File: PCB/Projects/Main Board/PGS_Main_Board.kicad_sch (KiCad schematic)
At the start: 119 parts, among them J1 SM02B-SURS-TF_LF__SN_, J2 SM02B-SURS-TF_LF__SN_, J3 Molex 505110-0892, J5 Molex 505110-0892, J6 Molex 505110-0492, J7 Molex 505110-0492, J8 Conn_01x04_Pin, J9 Molex 505110-1792, Q1 MMBT2222A, Q2 MMBT2222A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

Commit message: Main Board Update
- Put 1uF caps closer to designated pins
- Update timestamp on PCB mask
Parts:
- C18, C22: value 100nF -> 1uF; LCSC C160831 -> C76929; MPN CL03A104KQ3NNNC -> GRM033R60J105KEA2D; Manufacturer Samsung Electro-Mechanics -> Murata Electronics
- C3, C6: value 1uF -> 100nF; LCSC C76929 -> C160831; MPN GRM033R60J105KEA2D -> CL03A104KQ3NNNC; Manufacturer Murata Electronics -> Samsung Electro-Mechanics
- SW1, SW15, SW16, SW2, SW3, SW4: value TS-1187A-C-A-B -> TS-1187A-C-A-B

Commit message: Annotate schematic
1uF capacitor annotation updated for main PCB
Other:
- note added: "C11 1uF must be near pin 44"
- note added: "C18 1uF must be near pin 45"
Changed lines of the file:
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@@
+		)
+	)
+	(text "C18 1uF must be \nnear pin 45"
+		(exclude_from_sim no)
+		(at 44.45 68.072 0)
+		(effects
+			(font
+				(size 1.27 1.27)
+			)
 		)
 	)
@@
 		(effects
 			(font
+				(size 1.27 1.27)
+			)
+		)
+	)
+	(text "C11 1uF must be \nnear pin 44"
+		(exclude_from_sim no)
+		(at 115.062 84.582 0)
+		(effects
+			(font

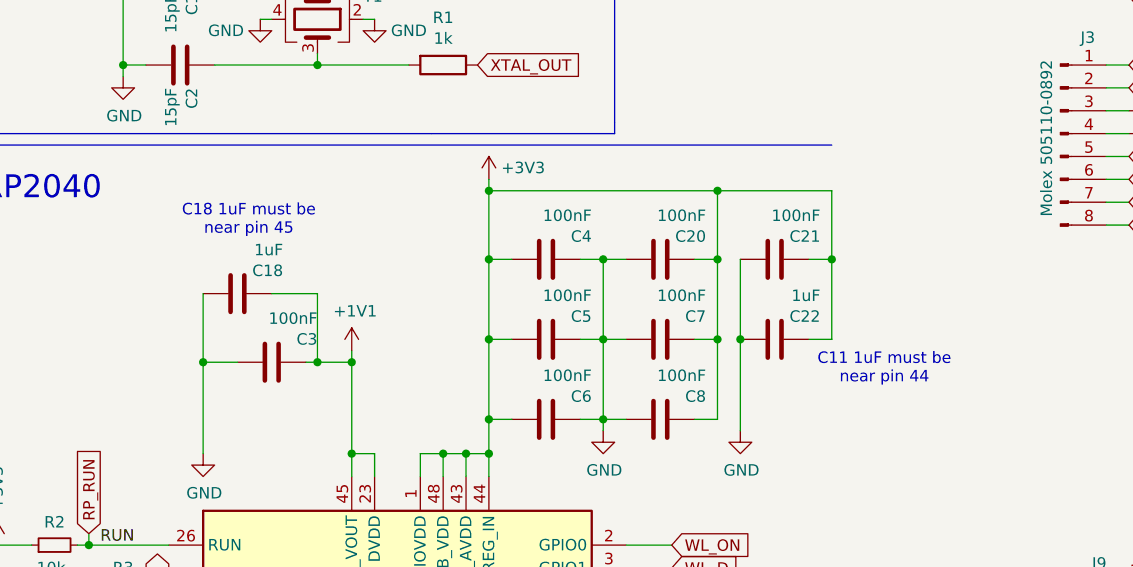
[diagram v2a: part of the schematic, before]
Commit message: USBW Update
- Implement fuel gauge IC
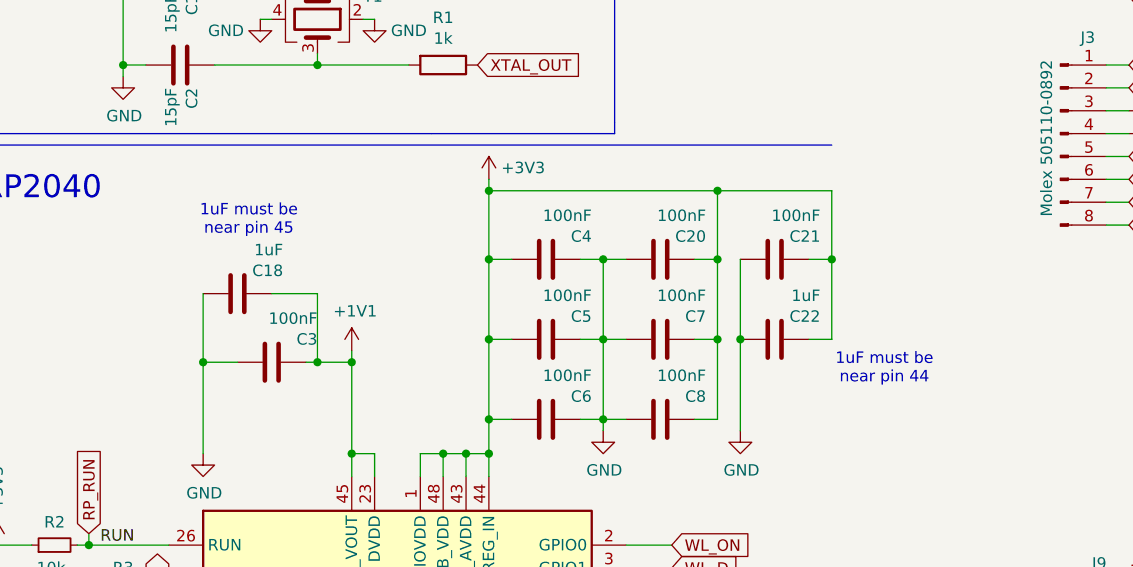
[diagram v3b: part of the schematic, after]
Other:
- note added: "1uF must be near pin 44"
- note added: "1uF must be near pin 45"
- note removed: "C11 1uF must be near pin 44"
- note removed: "C18 1uF must be near pin 45"
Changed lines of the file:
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@@
 		)
 	)
-	(text "C18 1uF must be \nnear pin 45"
+	(text "1uF must be \nnear pin 45"
 		(exclude_from_sim no)
 		(at 44.45 68.072 0)
@@
 		)
 	)
-	(text "C11 1uF must be \nnear pin 44"
+	(text "1uF must be \nnear pin 44"
 		(exclude_from_sim no)
 		(at 115.062 84.582 0)

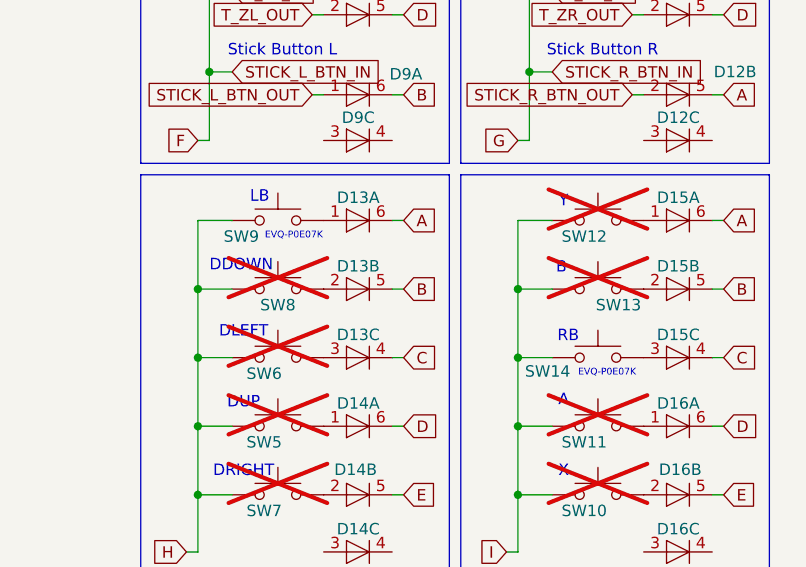
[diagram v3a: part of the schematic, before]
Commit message: Main Board/Trigger Board Update
- Main board updated with Kailh tactile switches
- Trigger board updated with Kailh tactile switches
- USBW board updated to remove unneeded diode, move position of USB-C port
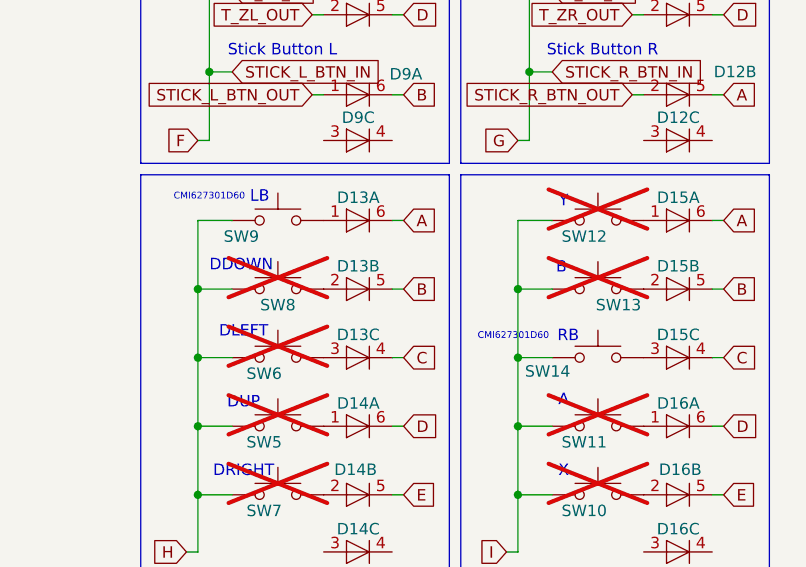
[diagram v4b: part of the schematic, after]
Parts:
- SW14, SW9: value EVQ-P0E07K -> CMI627301D60; LCSC C395225 -> (none); MPN EVQ-P0E07K -> CMI627301D60; Manufacturer PANASONIC -> Kailh
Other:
- note added: "CMI627301D60"
- note removed: "EVQ-P0E07K"
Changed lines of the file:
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@@
 		)
 	)
-	(text "EVQ-P0E07K"
+	(text "CMI627301D60"
 		(exclude_from_sim no)
-		(at 353.568 112.268 0)
+		(at 344.17 107.95 0)
 		(effects
 			(font
@@
 		)
 	)
-	(text "EVQ-P0E07K"
+	(text "CMI627301D60"
 		(exclude_from_sim no)
-		(at 388.366 127.508 0)
+		(at 377.952 123.444 0)
 		(effects
 			(font
@@
 			)
 		)
-		(property "Value" "EVQ-P0E07K"
+		(property "Value" "CMI627301D60"
 			(at 387.35 120.65 0)
 			(effects
@@
 			)
 		)
-		(property "MPN" "EVQ-P0E07K"
+		(property "MPN" "CMI627301D60"
 			(at 387.35 125.73 0)
 			(effects
@@
 			)
 		)
-		(property "LCSC" "C395225"
+		(property "LCSC" ""
 			(at 387.35 125.73 0)
 			(effects
@@
 			)
 		)
-		(property "Manufacturer" "PANASONIC"
+		(property "Manufacturer" "Kailh"
 			(at 387.35 125.73 0)
 			(effects
@@
 			)
 		)
-		(property "Value" "EVQ-P0E07K"
+		(property "Value" "CMI627301D60"
 			(at 351.79 105.41 0)
 			(effects
@@
 			)
 		)
-		(property "MPN" "EVQ-P0E07K"
+		(property "MPN" "CMI627301D60"
 			(at 351.79 110.49 0)
 			(effects
@@
 			)
 		)
-		(property "LCSC" "C395225"
+		(property "LCSC" ""
 			(at 351.79 110.49 0)
 			(effects
@@
 			)
 		)
-		(property "Manufacturer" "PANASONIC"
+		(property "Manufacturer" "Kailh"
 			(at 351.79 110.49 0)
 			(effects
